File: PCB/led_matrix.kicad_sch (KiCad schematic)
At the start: 66 parts

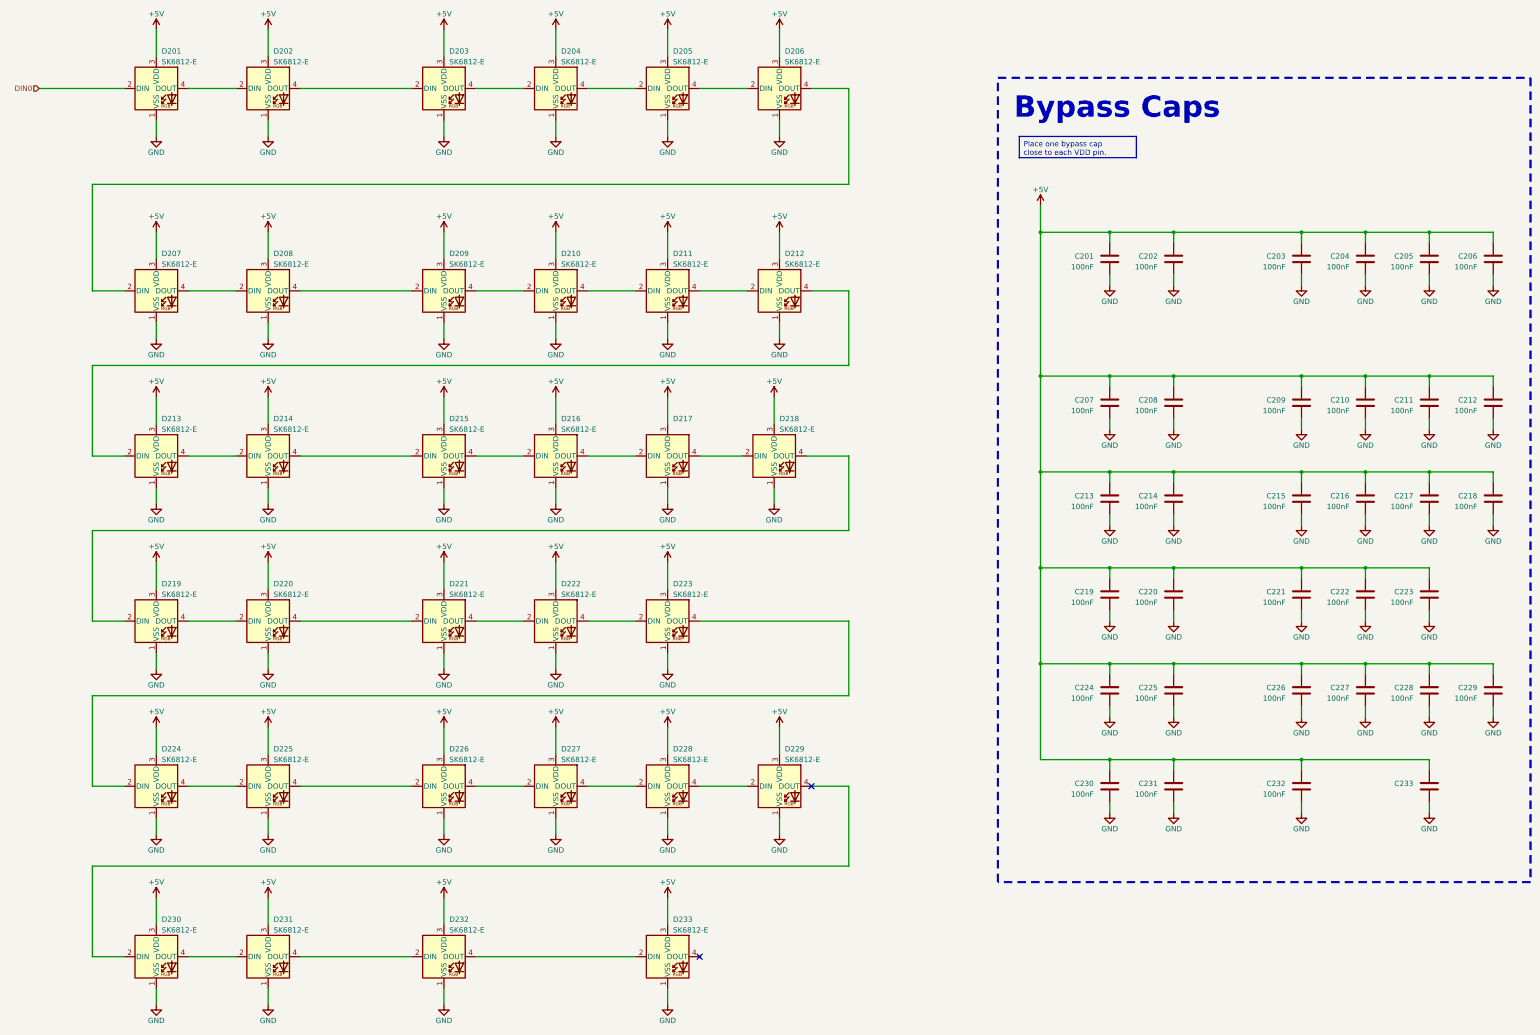
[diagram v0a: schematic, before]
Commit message: Fixed LED rotation, beefed up standoffs, added docs
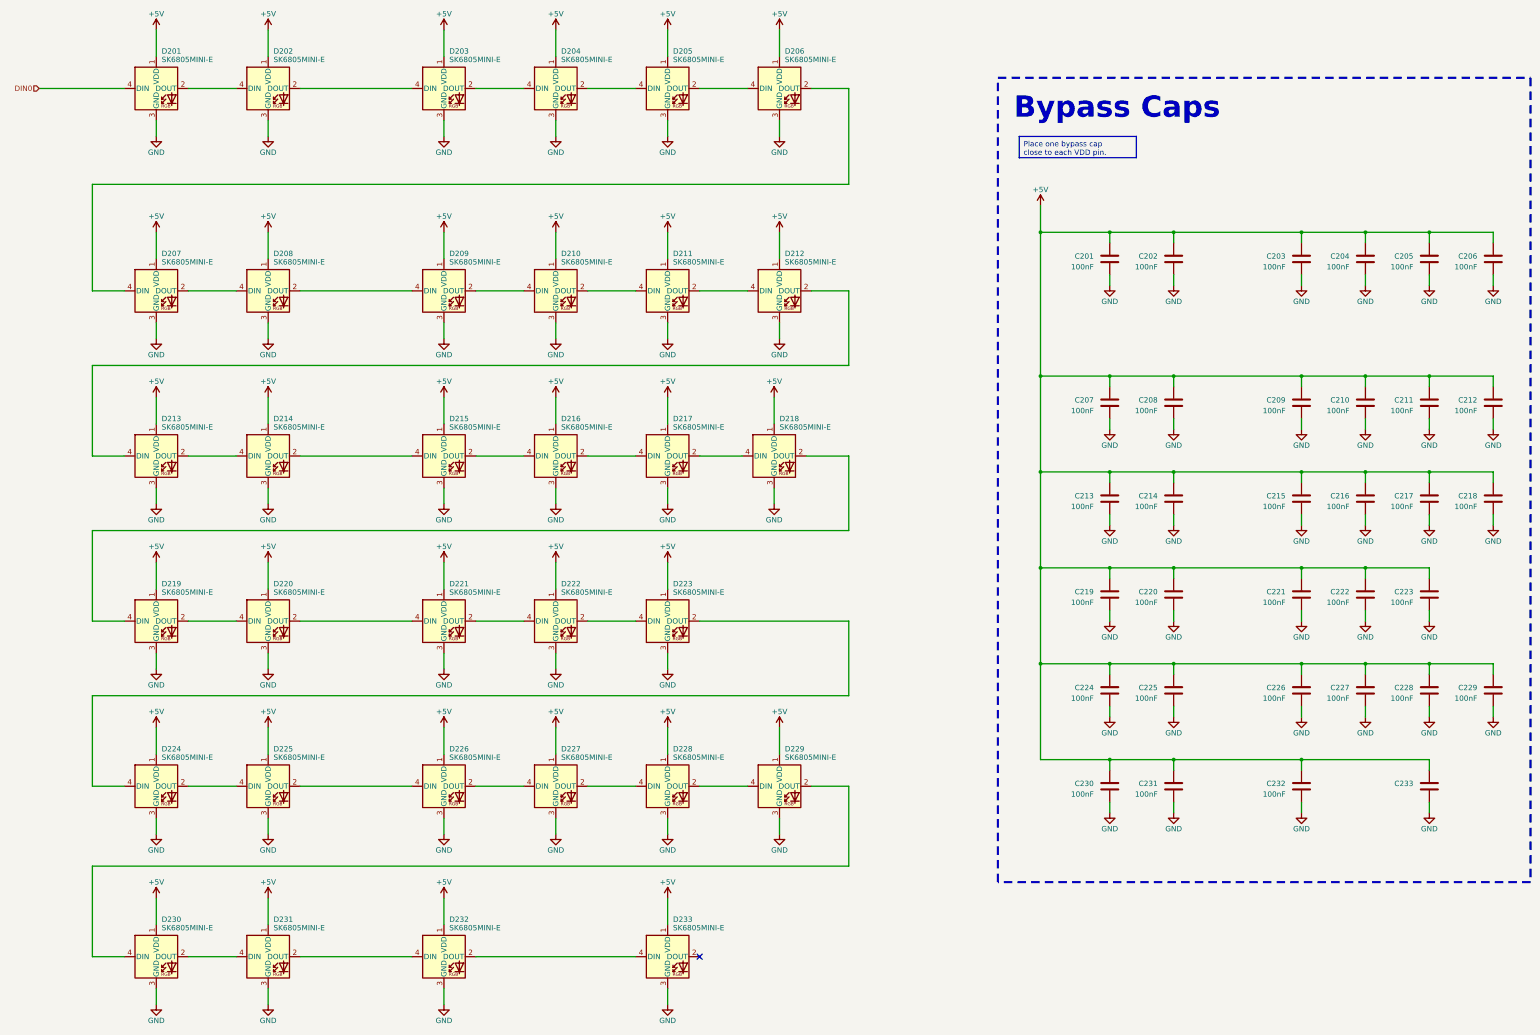
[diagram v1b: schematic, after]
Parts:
- D201, D202, D203, D204, D205, D206, D207, D208, D209, D210, D211, D212, D213, D214, D215, D216, D217, D218, D219, D220, D221, D222, D223, D224, D225, D226, D227, D228, D229, D230, D231, D232, D233: value SK6812-E -> SK6805MINI-E; symbol LED:SK6812 -> irex_LED:SK6805MINI-E
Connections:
- net +5V: now also D201.1 (VDD), D202.1 (VDD), D203.1 (VDD), D204.1 (VDD), D205.1 (VDD), D206.1 (VDD), D207.1 (VDD), D208.1 (VDD), D209.1 (VDD), D210.1 (VDD), D211.1 (VDD), D212.1 (VDD), D213.1 (VDD), D214.1 (VDD), D215.1 (VDD), D216.1 (VDD), D217.1 (VDD), D218.1 (VDD), D219.1 (VDD), D220.1 (VDD), D221.1 (VDD), D222.1 (VDD), D223.1 (VDD), D224.1 (VDD), D225.1 (VDD), D226.1 (VDD), D227.1 (VDD), D228.1 (VDD), D229.1 (VDD), D230.1 (VDD), D231.1 (VDD), D232.1 (VDD), D233.1 (VDD); no longer D201.3 (VDD), D202.3 (VDD), D203.3 (VDD), D204.3 (VDD), D205.3 (VDD), D206.3 (VDD), D207.3 (VDD), D208.3 (VDD), D209.3 (VDD), D210.3 (VDD), D211.3 (VDD), D212.3 (VDD), D213.3 (VDD), D214.3 (VDD), D215.3 (VDD), D216.3 (VDD), D217.3 (VDD), D218.3 (VDD), D219.3 (VDD), D220.3 (VDD), D221.3 (VDD), D222.3 (VDD), D223.3 (VDD), D224.3 (VDD), D225.3 (VDD), D226.3 (VDD), D227.3 (VDD), D228.3 (VDD), D229.3 (VDD), D230.3 (VDD), D231.3 (VDD), D232.3 (VDD), D233.3 (VDD)
- net DIN0: now also D201.4 (DIN); no longer D201.2 (DIN)
- net GND: now also D201.3 (GND), D202.3 (GND), D203.3 (GND), D204.3 (GND), D205.3 (GND), D206.3 (GND), D207.3 (GND), D208.3 (GND), D209.3 (GND), D210.3 (GND), D211.3 (GND), D212.3 (GND), D213.3 (GND), D214.3 (GND), D215.3 (GND), D216.3 (GND), D217.3 (GND), D218.3 (GND), D219.3 (GND), D220.3 (GND), D221.3 (GND), D222.3 (GND), D223.3 (GND), D224.3 (GND), D225.3 (GND), D226.3 (GND), D227.3 (GND), D228.3 (GND), D229.3 (GND), D230.3 (GND), D231.3 (GND), D232.3 (GND), D233.3 (GND); no longer D201.1 (VSS), D202.1 (VSS), D203.1 (VSS), D204.1 (VSS), D205.1 (VSS), D206.1 (VSS), D207.1 (VSS), D208.1 (VSS), D209.1 (VSS), D210.1 (VSS), D211.1 (VSS), D212.1 (VSS), D213.1 (VSS), D214.1 (VSS), D215.1 (VSS), D216.1 (VSS), D217.1 (VSS), D218.1 (VSS), D219.1 (VSS), D220.1 (VSS), D221.1 (VSS), D222.1 (VSS), D223.1 (VSS), D224.1 (VSS), D225.1 (VSS), D226.1 (VSS), D227.1 (VSS), D228.1 (VSS), D229.1 (VSS), D230.1 (VSS), D231.1 (VSS), D232.1 (VSS), D233.1 (VSS)
- net at D229.2 (DOUT): now also D230.4 (DIN); no longer D228.4 (DOUT)
- net at D229.4 (DIN): now also D228.2 (DOUT); no longer D230.2 (DIN)
- net at D227.2 (DOUT): now also D228.4 (DIN); no longer D226.4 (DOUT)
- net at D227.4 (DIN): now also D226.2 (DOUT); no longer D228.2 (DIN)
- net at D215.2 (DOUT): now also D216.4 (DIN); no longer D214.4 (DOUT)
- net at D215.4 (DIN): now also D214.2 (DOUT); no longer D216.2 (DIN)
- net at D210.2 (DOUT): now also D211.4 (DIN); no longer D209.4 (DOUT)
- net at D210.4 (DIN): now also D209.2 (DOUT); no longer D211.2 (DIN)
- net at D202.2 (DOUT): now also D203.4 (DIN); no longer D201.4 (DOUT)
- net at D202.4 (DIN): now also D201.2 (DOUT); no longer D203.2 (DIN)
- net at D212.2 (DOUT): now also D213.4 (DIN); no longer D211.4 (DOUT)
- net at D212.4 (DIN): now also D211.2 (DOUT); no longer D213.2 (DIN)
- net at D204.2 (DOUT): now also D205.4 (DIN); no longer D203.4 (DOUT)
- net at D204.4 (DIN): now also D203.2 (DOUT); no longer D205.2 (DIN)
- net at D206.2 (DOUT): now also D207.4 (DIN); no longer D205.4 (DOUT)
- net at D206.4 (DIN): now also D205.2 (DOUT); no longer D207.2 (DIN)
- net at D221.2 (DOUT): now also D222.4 (DIN); no longer D220.4 (DOUT)
- net at D221.4 (DIN): now also D220.2 (DOUT); no longer D222.2 (DIN)
- net at D219.2 (DOUT): now also D220.4 (DIN); no longer D218.4 (DOUT)
- net at D219.4 (DIN): now also D218.2 (DOUT); no longer D220.2 (DIN)
- net at D217.2 (DOUT): now also D218.4 (DIN); no longer D216.4 (DOUT)
- net at D208.2 (DOUT): now also D209.4 (DIN); no longer D207.4 (DOUT)
- net at D208.4 (DIN): now also D207.2 (DOUT); no longer D209.2 (DIN)
- net at D225.2 (DOUT): now also D226.4 (DIN); no longer D224.4 (DOUT)
- net at D225.4 (DIN): now also D224.2 (DOUT); no longer D226.2 (DIN)
- net at D233.2 (DOUT): no longer D232.4 (DOUT)
- net at D233.4 (DIN): now also D232.2 (DOUT)
- net at D223.4 (DIN): now also D222.2 (DOUT); no longer D224.2 (DIN)
- net at D223.2 (DOUT): now also D224.4 (DIN); no longer D222.4 (DOUT)
- net at D217.4 (DIN): now also D216.2 (DOUT); no longer D218.2 (DIN)
- net at D231.2 (DOUT): now also D232.4 (DIN); no longer D230.4 (DOUT)
- net at D231.4 (DIN): now also D230.2 (DOUT); no longer D232.2 (DIN)
- new net: D213.2 (DOUT), D214.4 (DIN)
- no-connect marks 2 -> 1
